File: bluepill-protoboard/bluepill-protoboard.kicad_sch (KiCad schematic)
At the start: 15 parts, among them J1 Conn_01x20_Socket, J10 Conn_01x04_Pin, J11 Conn_01x04_Pin, J13 Conn_01x06_Pin, J14 Conn_01x04_Pin, J15 Conn_01x04_Pin, J2 Conn_01x17_Pin, J3 Conn_01x17_Pin, J4 Conn_01x17_Pin, J5 Conn_01x04_Pin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

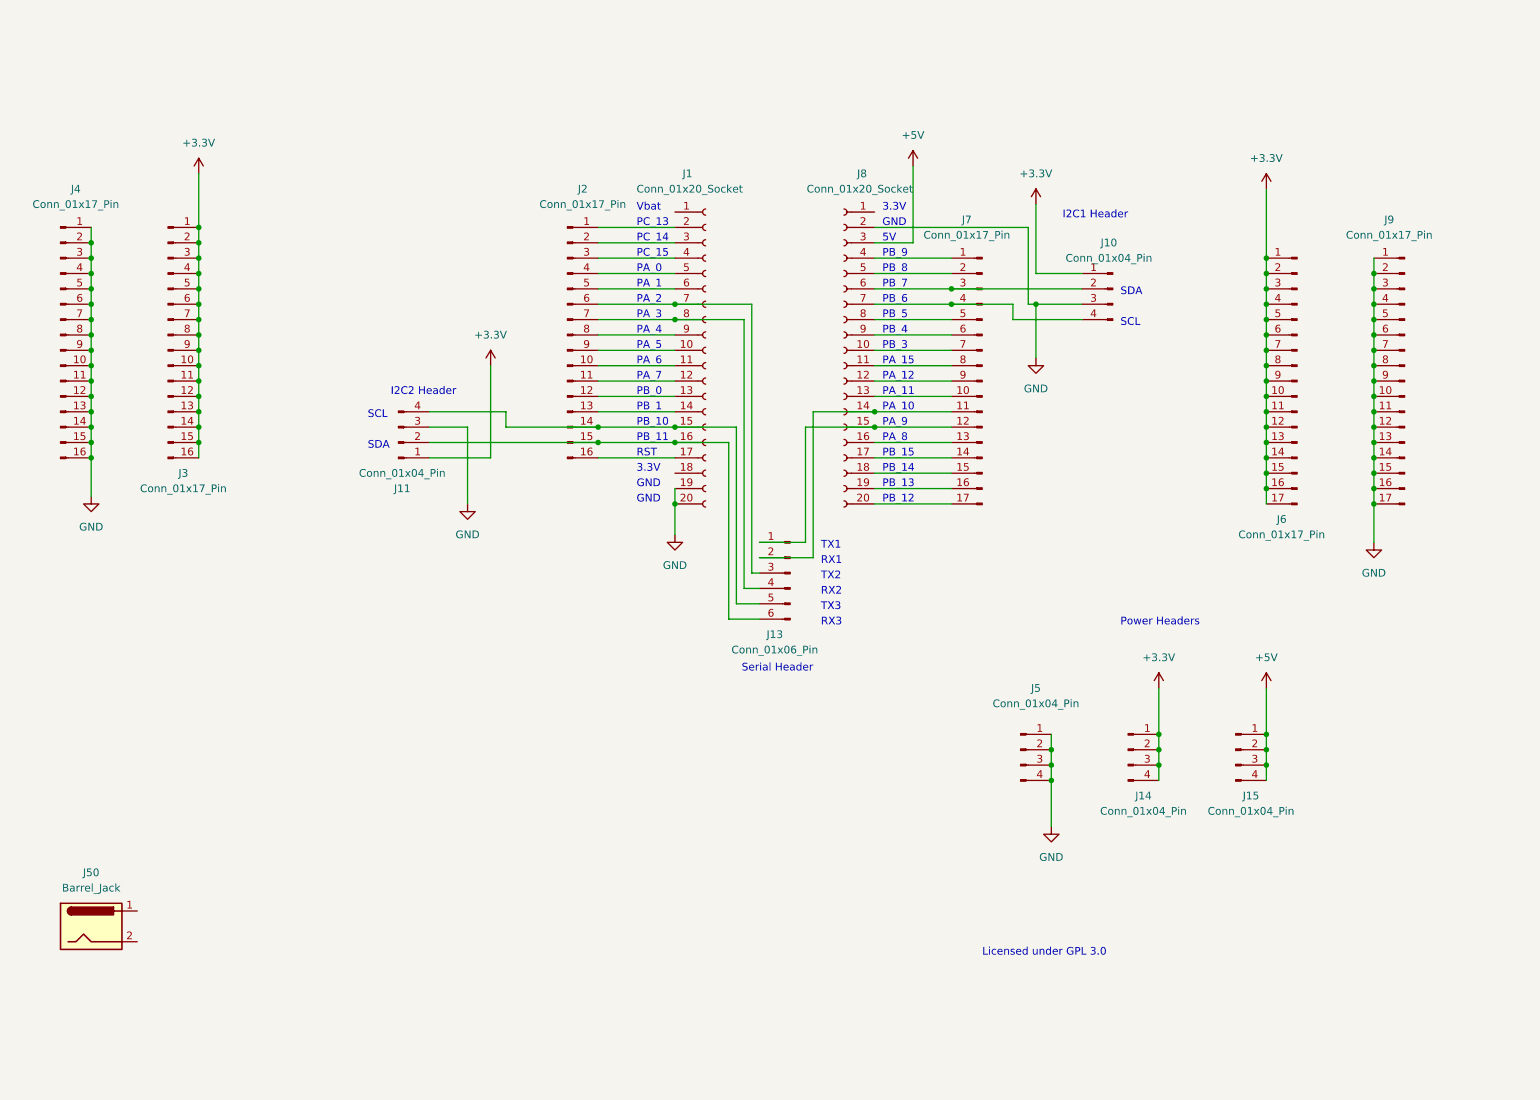
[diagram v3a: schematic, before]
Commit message: Add regulator drafts
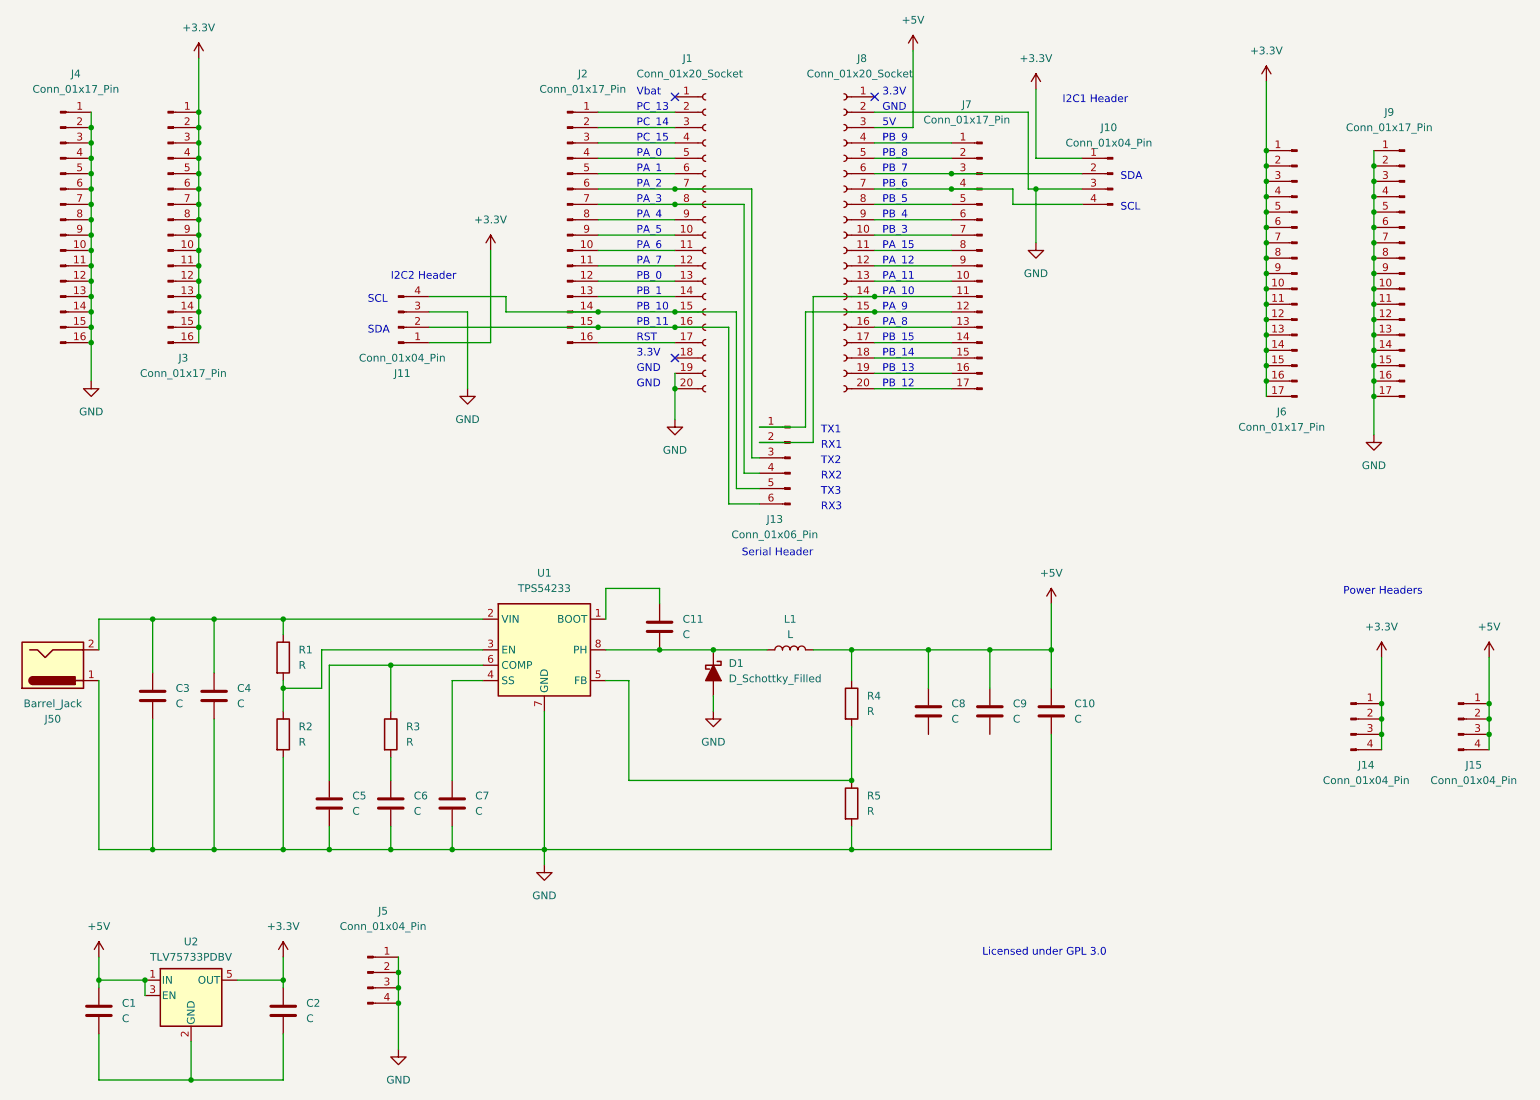
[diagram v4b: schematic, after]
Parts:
- added C1, C10, C11, C2, C3, C4, C5, C6, C7, C8, C9: C, symbol Device:C
- added D1: D_Schottky_Filled, symbol Device:D_Schottky_Filled
- added L1: L, symbol Device:L
- added R1, R2, R3, R4, R5: R, symbol Device:R
- added U1: TPS54233, Package_SO:SOIC-8_3.9x4.9mm_P1.27mm, symbol Regulator_Switching:TPS54233
- added U2: TLV75733PDBV, Package_TO_SOT_SMD:SOT-23-5, symbol Regulator_Linear:TLV75733PDBV
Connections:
- net +3.3V: now also C2.1, U2.5 (OUT)
- net +5V: now also C1.1, C10.1, C8.1, C9.1, L1.2, R4.1, U2.1 (IN), U2.3 (EN)
- net GND: now also J50.1, C10.2, C3.2, C4.2, C5.2, C6.2, C7.2, D1.2 (A), R2.2, R5.2, U1.7 (GND)
- net at J50.2: now also C3.1, C4.1, R1.1, U1.2 (VIN)
- new net: C11.2, D1.1 (K), L1.1, U1.8 (PH)
- new net: C5.1, R3.1, U1.6 (COMP)
- new net: C1.2, C2.2, U2.2 (GND)
- new net: C11.1, U1.1 (BOOT)
- new net: R1.2, R2.1, U1.3 (EN)
- new net: R4.2, R5.1, U1.5 (FB)
- new net: C7.1, U1.4 (SS)
- new net: C6.1, R3.2
- no-connect marks 0 -> 3
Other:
- moved on the sheet: J1, J10, J11, J13, J14, J15, J2, J3, J4, J5, J50, J6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

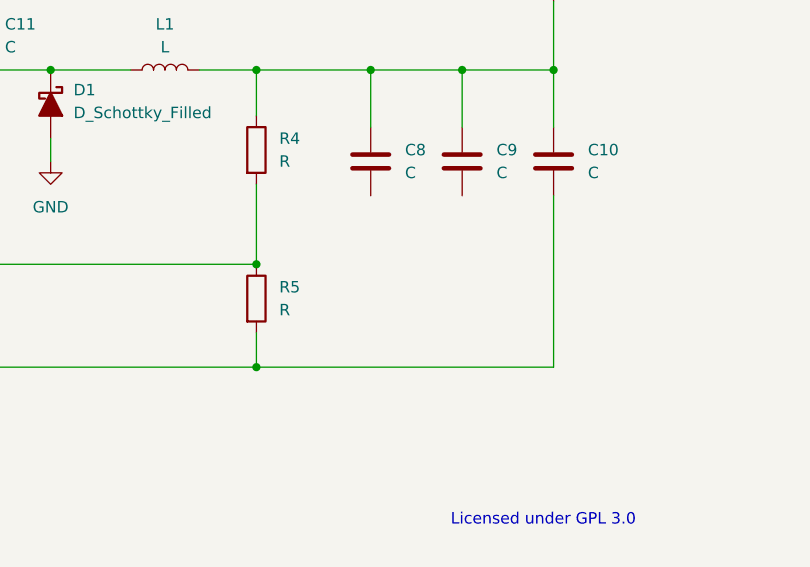
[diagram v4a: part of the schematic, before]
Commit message: Add missed connections
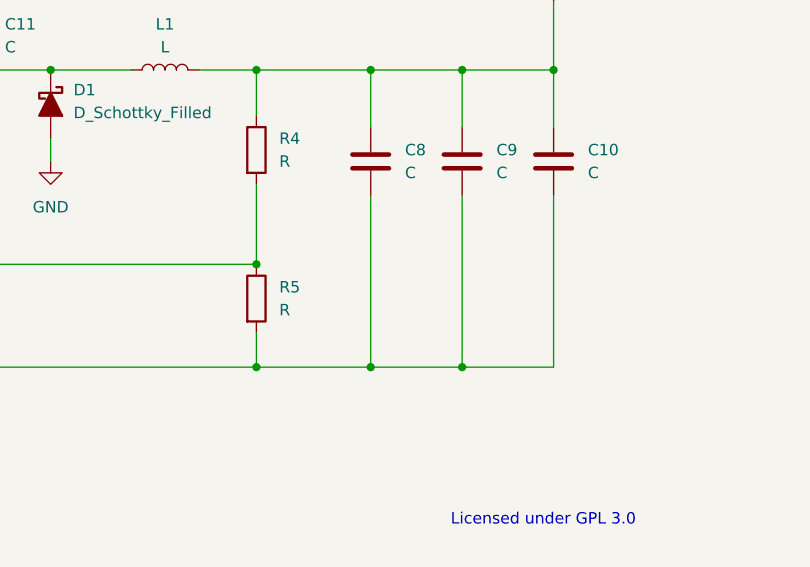
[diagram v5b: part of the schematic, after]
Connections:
- net GND: now also C8.2, C9.2
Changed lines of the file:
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@@
   (junction (at 49.53 55.88) (diameter 0) (color 0 0 0 0)
   )
+  (junction (at 180.34 152.4) (diameter 0) (color 0 0 0 0)
+  )
   (junction (at 157.48 140.97) (diameter 0) (color 0 0 0 0)
   )
@@
   )
   (junction (at 71.12 152.4) (diameter 0) (color 0 0 0 0)
+  )
+  (junction (at 170.18 152.4) (diameter 0) (color 0 0 0 0)
   )
   (junction (at 262.89 128.27) (diameter 0) (color 0 0 0 0)
@@
     (stroke (width 0) (type default))
   )
+  (wire (pts (xy 180.34 133.35) (xy 180.34 152.4))
+    (stroke (width 0) (type default))
+  )
   (wire (pts (xy 115.57 30.48) (xy 128.27 30.48))
     (stroke (width 0) (type default))
   )
+  (wire (pts (xy 170.18 152.4) (xy 157.48 152.4))
+    (stroke (width 0) (type default))
+  )
   (wire (pts (xy 49.53 43.18) (xy 49.53 45.72))
     (stroke (width 0) (type default))
@@
     (stroke (width 0) (type default))
   )
-  (wire (pts (xy 190.5 152.4) (xy 157.48 152.4))
+  (wire (pts (xy 190.5 152.4) (xy 180.34 152.4))
     (stroke (width 0) (type default))
   )
@@
     (stroke (width 0) (type default))
   )
+  (wire (pts (xy 180.34 152.4) (xy 170.18 152.4))
+    (stroke (width 0) (type default))
+  )
   (wire (pts (xy 116.84 119.38) (xy 125.73 119.38))
     (stroke (width 0) (type default))
@@
     (stroke (width 0) (type default))
   )
+  (wire (pts (xy 170.18 133.35) (xy 170.18 152.4))
+    (stroke (width 0) (type default))
+  )
